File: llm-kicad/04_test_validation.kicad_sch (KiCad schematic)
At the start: 27 parts

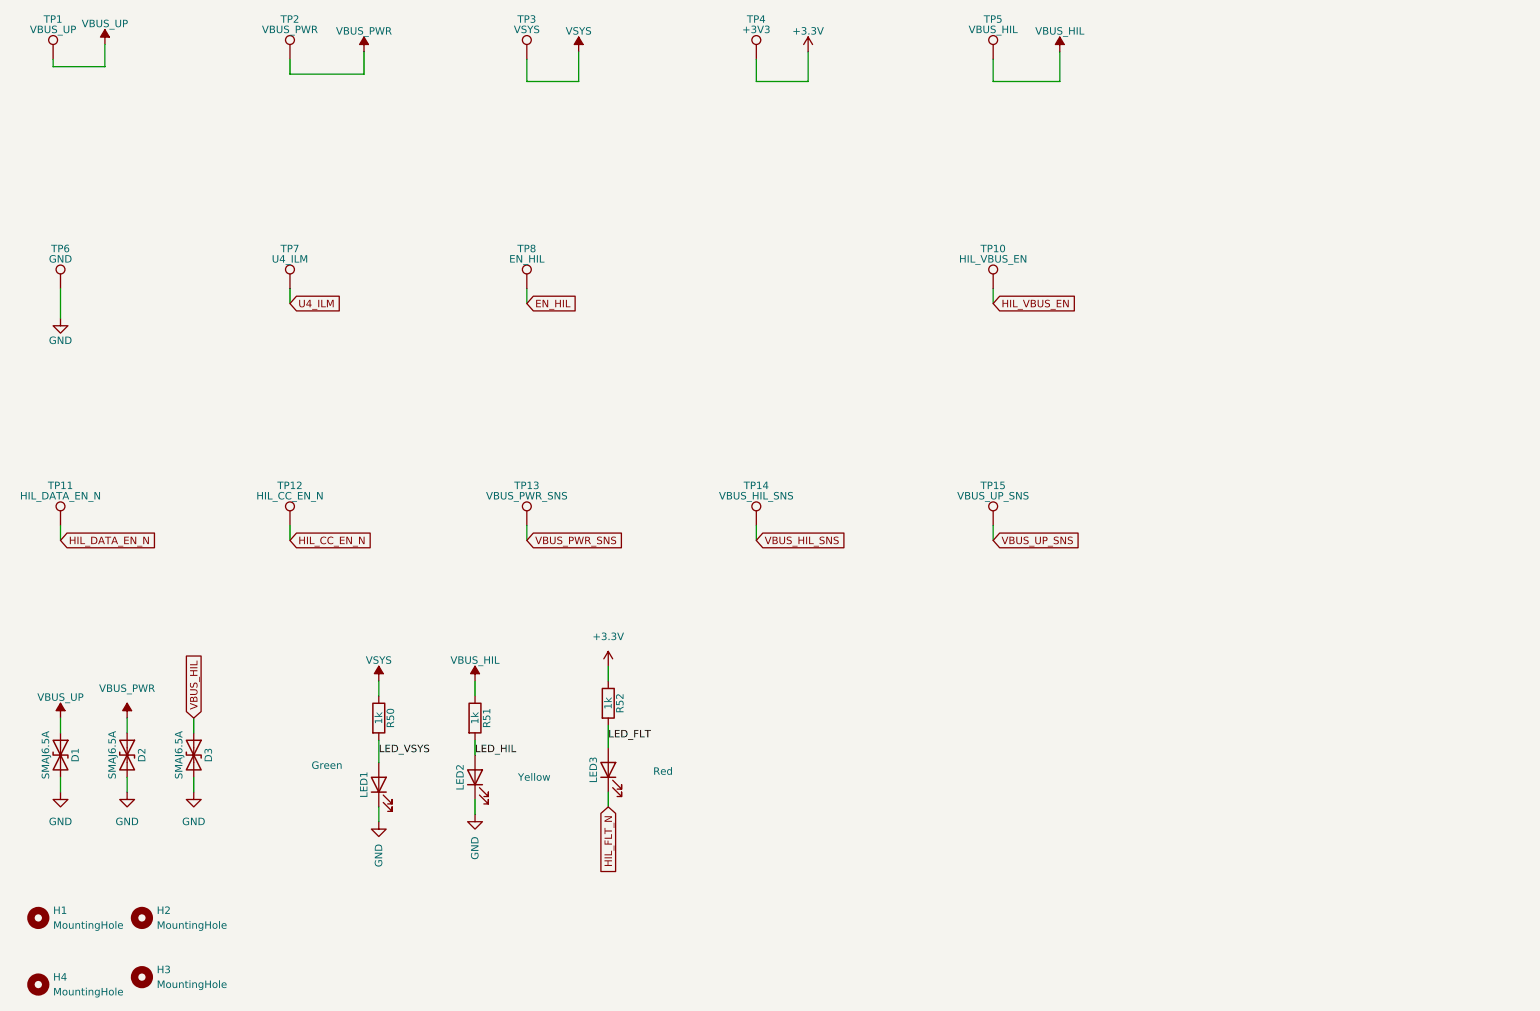
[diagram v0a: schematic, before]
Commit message: Fixed incorrect footprint and added external GPIO
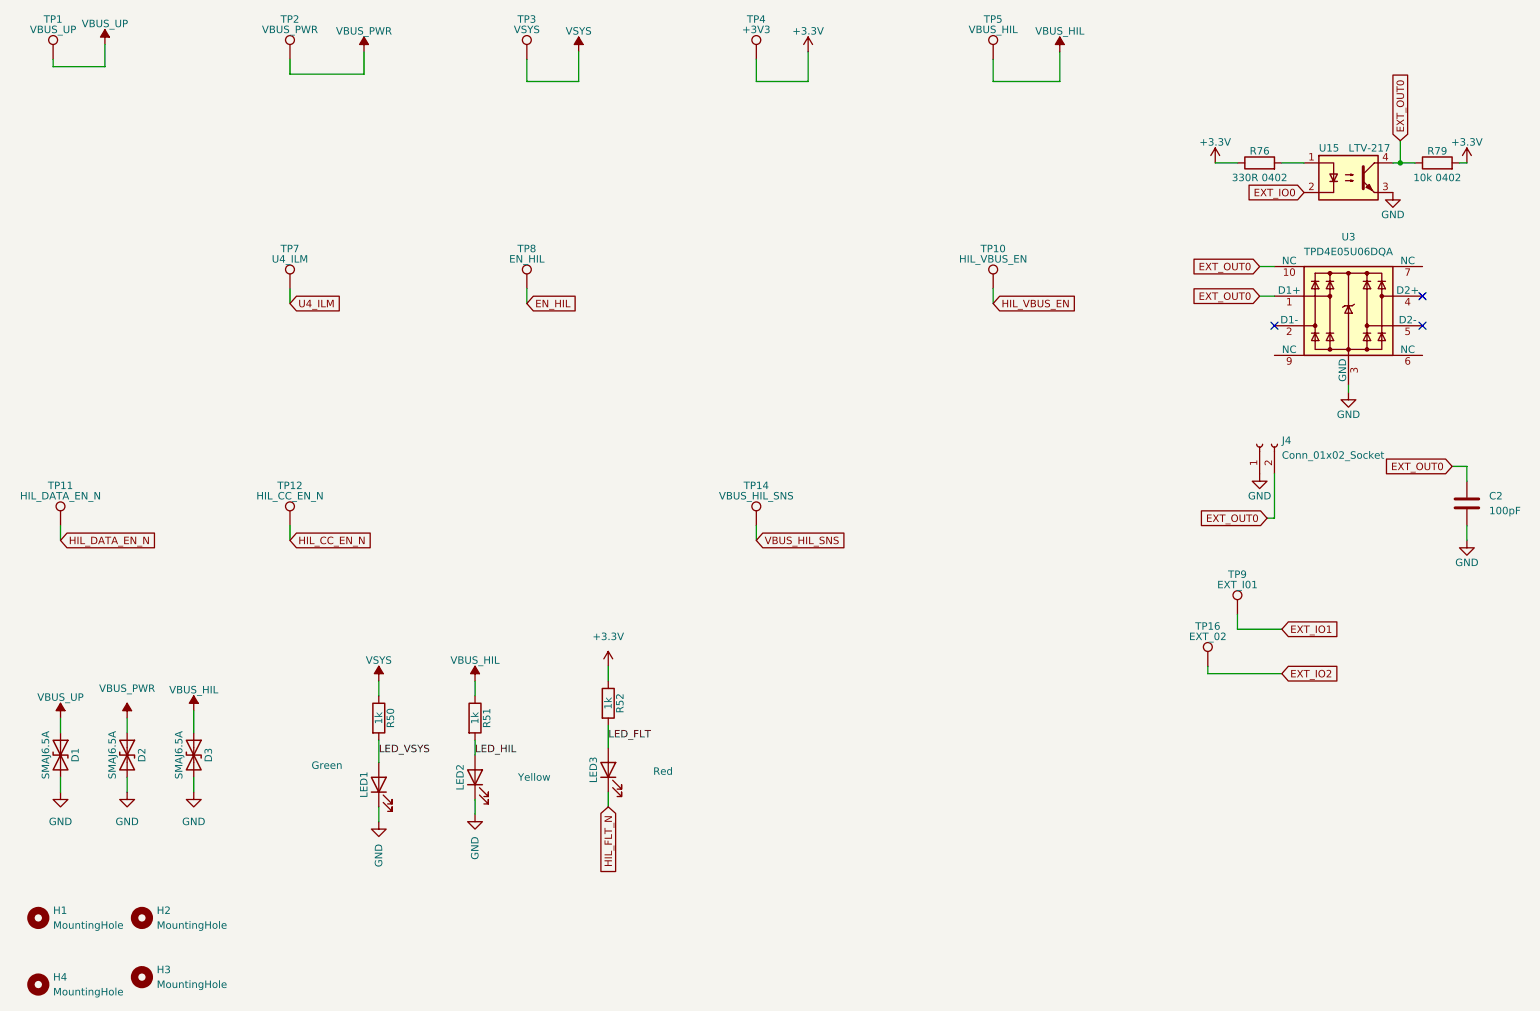
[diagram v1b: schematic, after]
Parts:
- removed TP13: VBUS_PWR_SNS, TestPoint:TestPoint_Pad_D1.5mm, symbol Connector:TestPoint
- removed TP15: VBUS_UP_SNS, TestPoint:TestPoint_Pad_D1.5mm, symbol Connector:TestPoint
- removed TP6: GND, TestPoint:TestPoint_Pad_D1.5mm, symbol Connector:TestPoint
- added C2: 100pF, Capacitor_SMD:C_0402_1005Metric, symbol Device:C
- added J4: Conn_01x02_Socket, Connector_PinHeader_2.54mm:PinHeader_1x02_P2.54mm_Vertical, symbol Connector:Conn_01x02_Socket
- added R76: 330R 0402, Resistor_SMD:R_0402_1005Metric, symbol Device:R
- added R79: 10k 0402, Resistor_SMD:R_0402_1005Metric, symbol Device:R
- added TP16: EXT_02, TestPoint:TestPoint_Pad_D1.5mm, symbol Connector:TestPoint
- added TP9: EXT_I01, TestPoint:TestPoint_Pad_D1.5mm, symbol Connector:TestPoint
- added U15: LTV-217, Package_SO:SOP-4_4.4x2.6mm_P1.27mm, symbol Isolator:PC817
- added U3: TPD4E05U06DQA, Package_SON:USON-10_2.5x1.0mm_P0.5mm, symbol Power_Protection:TPD4E05U06DQA
- TP5: footprint TestPoint:TestPoint_Pad_D1.5mm -> TestPoint:TestPoint_Pad_D2.0mm
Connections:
- net +3.3V: now also R76.1, R79.2
- net GND: now also C2.2, J4.1 (Pin_1), U15.3, U3.3 (GND), U3.8 (GND)
- new net: R76.2, U15.1
- new net EXT_IO0: U15.2
- new net EXT_IO1: TP9.1
- new net EXT_IO2: TP16.1
- new net EXT_OUT0: C2.1, J4.2 (Pin_2), R79.1, U15.4, U3.1 (D1+), U3.10 (NC)
- no-connect marks 0 -> 3

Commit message: Ready for first production
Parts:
- J4: now left out of the parts list
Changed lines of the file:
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@@
 		(body_style 1)
 		(exclude_from_sim no)
-		(in_bom yes)
+		(in_bom no)
 		(on_board yes)
 		(in_pos_files yes)

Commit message: Fixed namning of some components
Remove footprint name
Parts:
- R76: value 330R 0402 -> 330R
- R79: value 10k 0402 -> 10k
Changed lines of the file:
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@@
 			)
 		)
-		(property "Value" "10k 0402"
+		(property "Value" "10k"
 			(at 266.7 50.8 90)
 			(show_name no)
@@
 			)
 		)
-		(property "Value" "330R 0402"
+		(property "Value" "330R"
 			(at 236.22 50.8 90)
 			(show_name no)
